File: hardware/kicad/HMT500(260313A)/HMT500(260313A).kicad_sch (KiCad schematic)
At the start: 0 parts

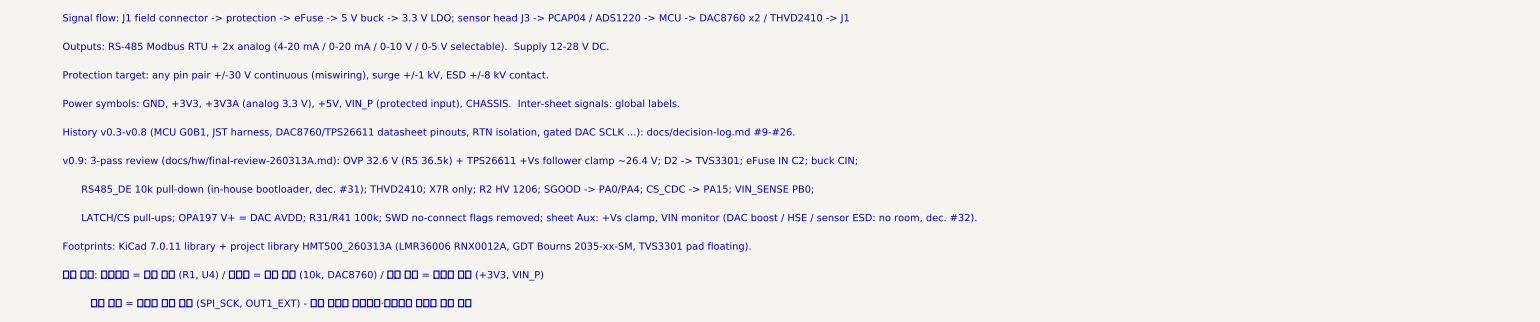
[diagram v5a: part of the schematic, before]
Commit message: Apply agreed external review items (decision #35)
- H01: series 100 V Schottky D3 (PMEG10010ELR) between D2 and eFuse IN
  (new net VIN_D) so negative surges no longer stress U1 IN-OUT
- H02: RS-485 bus TVS D60/D61 (TVS3301); U11 -> THVD2410DGKR (VSSOP-8)
- H04: +Vs clamp zener 27 V -> 24 V (BZX84C24LT1G)
- H08: ADS1220 IDAC fixed at 250 uA
- Room for new parts: C7 removed, 37 low-voltage R/C moved to 0402
  (LCSC basic where available); chassis parts keep CH_GAP between each other
- Placement 104/104, netlist 78/78, pcbnew DRC: no clearance errors,
  assembly sim 23 OK; parts list / JLC BOM updated
- docs/hw/external-review-response-260930.md: item responses, output load
  table, current budget, firmware requirements F1-F6, tests T1-T7

Co-Authored-By: Claude Opus 5.5 <noreply@anthropic.com>
Claude-Session: https://claude.ai/code/session_01JA2o8uJsqp9Vzsg4b665ev
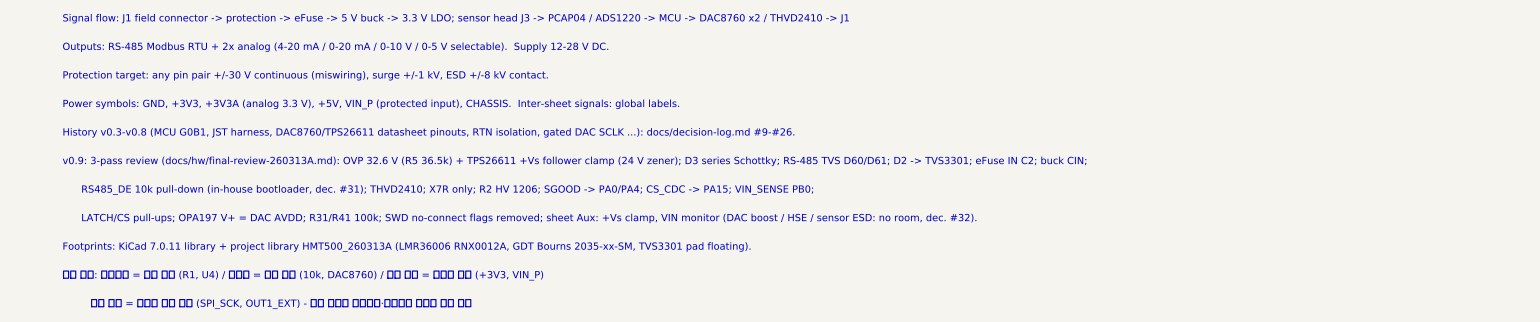
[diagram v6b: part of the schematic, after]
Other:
- note added: "v0.9: 3-pass review (docs/hw/final-review-260313A.md): OVP 32.6 V (R5 36.5k) + TPS26611 +Vs follower clamp (24 V zener); D3 series Schottky; RS-485 TVS D60/D61; D2 -> TVS3301; eFuse IN C2; buck CIN;"
- note removed: "v0.9: 3-pass review (docs/hw/final-review-260313A.md): OVP 32.6 V (R5 36.5k) + TPS26611 +Vs follower clamp ~26.4 V; D2 -> TVS3301; eFuse IN C2; buck CIN;"
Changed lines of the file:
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@@
 (text "Power symbols: GND, +3V3, +3V3A (analog 3.3 V), +5V, VIN_P (protected input), CHASSIS.  Inter-sheet signals: global labels." (at 30.48 177.8 0) (effects (font (size 1.4 1.4)) (justify left bottom)))
 (text "History v0.3-v0.8 (MCU G0B1, JST harness, DAC8760/TPS26611 datasheet pinouts, RTN isolation, gated DAC SCLK ...): docs/decision-log.md #9-#26." (at 30.48 183.388 0) (effects (font (size 1.4 1.4)) (justify left bottom)))
-(text "v0.9: 3-pass review (docs/hw/final-review-260313A.md): OVP 32.6 V (R5 36.5k) + TPS26611 +Vs follower clamp ~26.4 V; D2 -> TVS3301; eFuse IN C2; buck CIN;" (at 30.48 188.976 0) (effects (font (size 1.4 1.4)) (justify left bottom)))
+(text "v0.9: 3-pass review (docs/hw/final-review-260313A.md): OVP 32.6 V (R5 36.5k) + TPS26611 +Vs follower clamp (24 V zener); D3 series Schottky; RS-485 TVS D60/D61; D2 -> TVS3301; eFuse IN C2; buck CIN;" (at 30.48 188.976 0) (effects (font (size 1.4 1.4)) (justify left bottom)))
 (text "      RS485_DE 10k pull-down (in-house bootloader, dec. #31); THVD2410; X7R only; R2 HV 1206; SGOOD -> PA0/PA4; CS_CDC -> PA15; VIN_SENSE PB0;" (at 30.48 194.564 0) (effects (font (size 1.4 1.4)) (justify left bottom)))
 (text "      LATCH/CS pull-ups; OPA197 V+ = DAC AVDD; R31/R41 100k; SWD no-connect flags removed; sheet Aux: +Vs clamp, VIN monitor (DAC boost / HSE / sensor ESD: no room, dec. #32)." (at 30.48 200.152 0) (effects (font (size 1.4 1.4)) (justify left bottom)))

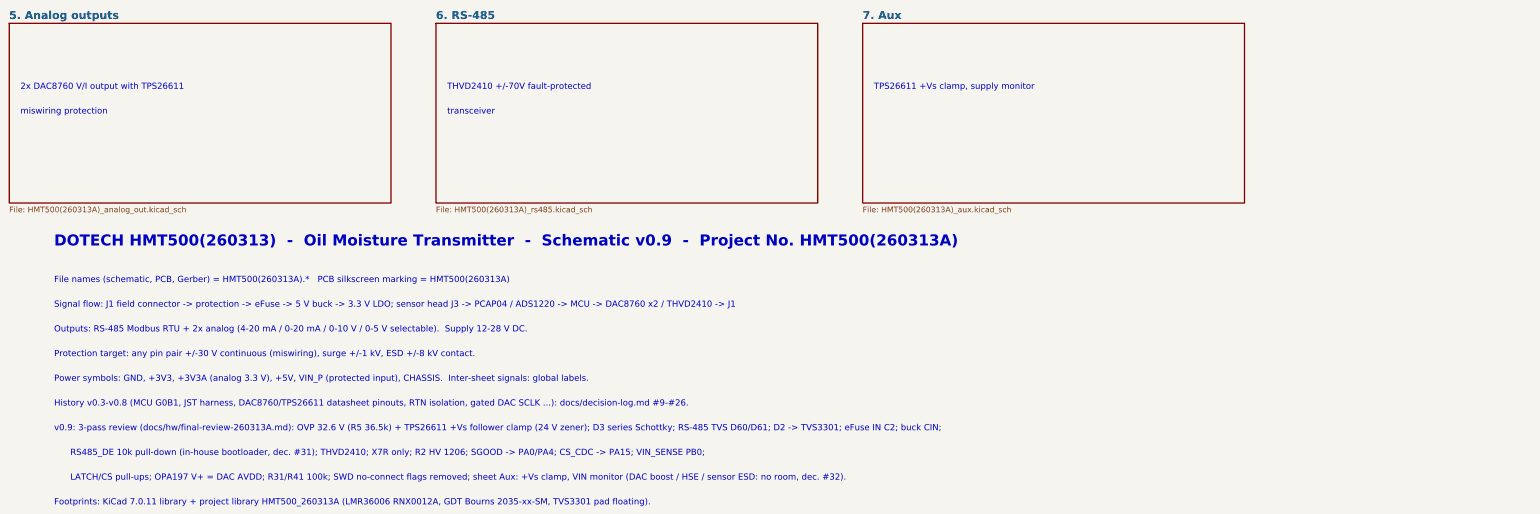
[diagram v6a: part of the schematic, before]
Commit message: Decision #37: fix the DAC section with the IVS320 AO rev 1.0 scheme
- AO supply VAO 16.1 V: LMR51606YFDBVR buck (U15) + 22 uH + 2x10 uF,
  feeding DAC AVDD (via 10 ohm), TPS26611 +Vs and OPA197 V+
- Remove +Vs zener follower (Q1, R50, D50, C53) and C43
- DAC CMP compensation 4.7 nF VOUT-CMP + 100 pF CMP-GND (SBAS528D 8.3.2)
- DAC output clamp BAS70-04 (D41/D51) for protector switching transients
- Output TVS3301 and SGOOD -> MCU ADC kept (+-30 V miswiring requirement)
- 114/114 parts placed, netlist 82/82, DRC no clearance errors,
  assembly sim 23 OK; parts list, JLC BOM, review docs updated

Co-Authored-By: Claude Opus 5.5 <noreply@anthropic.com>
Claude-Session: https://claude.ai/code/session_01JA2o8uJsqp9Vzsg4b665ev
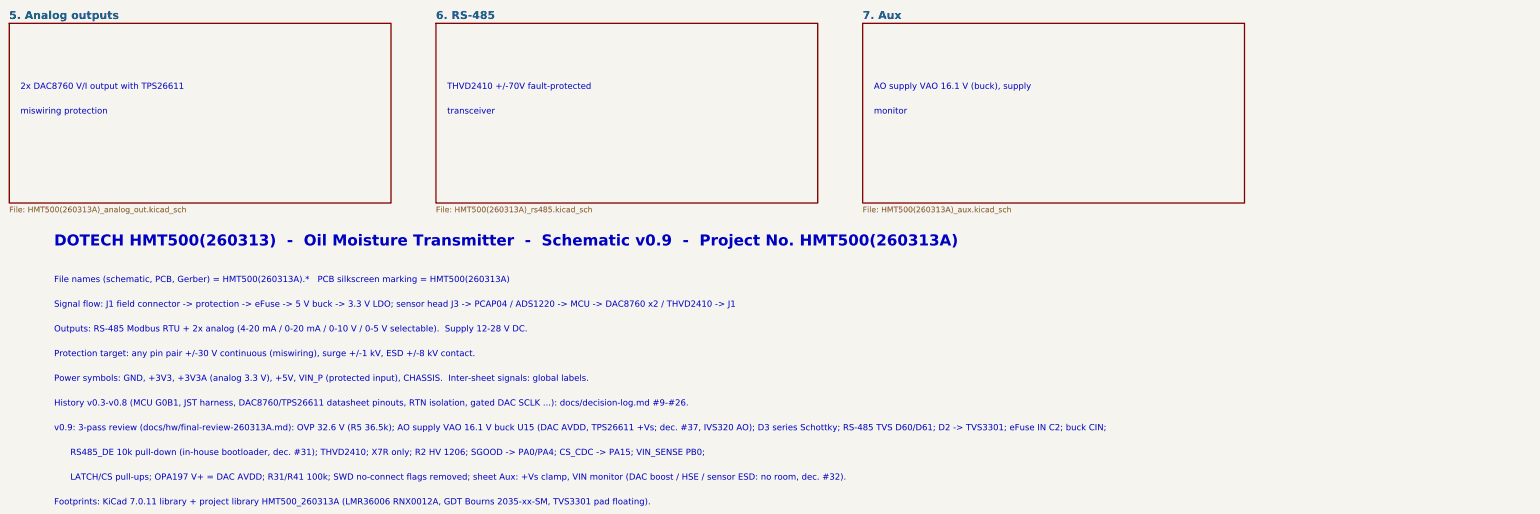
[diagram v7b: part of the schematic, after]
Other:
- note added: "AO supply VAO 16.1 V (buck), supply"
- note added: "monitor"
- note added: "v0.9: 3-pass review (docs/hw/final-review-260313A.md): OVP 32.6 V (R5 36.5k); AO supply VAO 16.1 V buck U15 (DAC AVDD, TPS26611 +Vs; dec. #37, IVS320 AO); D3 series Schottky; RS-485 TVS D60/D61; D2 -> TVS3301; eFuse IN C2; buck CIN;"
- note removed: "TPS26611 +Vs clamp, supply monitor"
- note removed: "v0.9: 3-pass review (docs/hw/final-review-260313A.md): OVP 32.6 V (R5 36.5k) + TPS26611 +Vs follower clamp (24 V zener); D3 series Schottky; RS-485 TVS D60/D61; D2 -> TVS3301; eFuse IN C2; buck CIN;"
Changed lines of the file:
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@@
 (text "transceiver" (at 119.38 117.348 0) (effects (font (size 1.4 1.4)) (justify left bottom)))
 (sheet (at 213.36 96.52) (size 86.36 40.64) (fields_autoplaced) (stroke (width 0.1524) (type solid)) (fill (color 0 0 0 0.0000)) (property "Sheetname" "7. Aux" (at 213.36 95.758 0) (effects (font (size 1.8 1.8) bold) (justify left bottom))) (property "Sheetfile" "HMT500(260313A)_aux.kicad_sch" (at 213.36 137.922 0) (effects (font (size 1.27 1.27)) (justify left top))) (instances (project "HMT500(260313A)" (path "/1ebb025b-11bd-5f7c-aaab-41e2a750e8b3" (page "8")))))
-(text "TPS26611 +Vs clamp, supply monitor" (at 215.9 111.76 0) (effects (font (size 1.4 1.4)) (justify left bottom)))
+(text "AO supply VAO 16.1 V (buck), supply" (at 215.9 111.76 0) (effects (font (size 1.4 1.4)) (justify left bottom)))
+(text "monitor" (at 215.9 117.348 0) (effects (font (size 1.4 1.4)) (justify left bottom)))
 (text "DOTECH HMT500(260313)  -  Oil Moisture Transmitter  -  Schematic v0.9  -  Project No. HMT500(260313A)" (at 30.48 147.32 0) (effects (font (size 2.5 2.5) bold) (justify left bottom)))
 (text "File names (schematic, PCB, Gerber) = HMT500(260313A).*   PCB silkscreen marking = HMT500(260313A)" (at 30.48 155.448 0) (effects (font (size 1.4 1.4)) (justify left bottom)))
@@
 (text "Power symbols: GND, +3V3, +3V3A (analog 3.3 V), +5V, VIN_P (protected input), CHASSIS.  Inter-sheet signals: global labels." (at 30.48 177.8 0) (effects (font (size 1.4 1.4)) (justify left bottom)))
 (text "History v0.3-v0.8 (MCU G0B1, JST harness, DAC8760/TPS26611 datasheet pinouts, RTN isolation, gated DAC SCLK ...): docs/decision-log.md #9-#26." (at 30.48 183.388 0) (effects (font (size 1.4 1.4)) (justify left bottom)))
-(text "v0.9: 3-pass review (docs/hw/final-review-260313A.md): OVP 32.6 V (R5 36.5k) + TPS26611 +Vs follower clamp (24 V zener); D3 series Schottky; RS-485 TVS D60/D61; D2 -> TVS3301; eFuse IN C2; buck CIN;" (at 30.48 188.976 0) (effects (font (size 1.4 1.4)) (justify left bottom)))
+(text "v0.9: 3-pass review (docs/hw/final-review-260313A.md): OVP 32.6 V (R5 36.5k); AO supply VAO 16.1 V buck U15 (DAC AVDD, TPS26611 +Vs; dec. #37, IVS320 AO); D3 series Schottky; RS-485 TVS D60/D61; D2 -> TVS3301; eFuse IN C2; buck CIN;" (at 30.48 188.976 0) (effects (font (size 1.4 1.4)) (justify left bottom)))
 (text "      RS485_DE 10k pull-down (in-house bootloader, dec. #31); THVD2410; X7R only; R2 HV 1206; SGOOD -> PA0/PA4; CS_CDC -> PA15; VIN_SENSE PB0;" (at 30.48 194.564 0) (effects (font (size 1.4 1.4)) (justify left bottom)))
 (text "      LATCH/CS pull-ups; OPA197 V+ = DAC AVDD; R31/R41 100k; SWD no-connect flags removed; sheet Aux: +Vs clamp, VIN monitor (DAC boost / HSE / sensor ESD: no room, dec. #32)." (at 30.48 200.152 0) (effects (font (size 1.4 1.4)) (justify left bottom)))

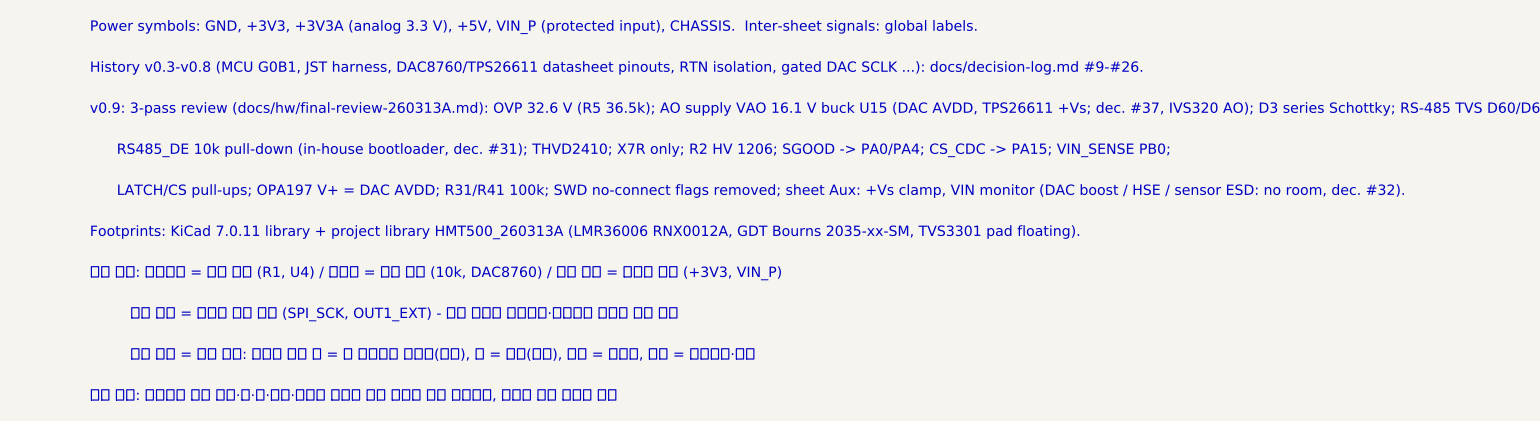
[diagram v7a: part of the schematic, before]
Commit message: Decision #38: prefer JLCPCB parts - U2 LMR51606, R19 0.1 %, std 2512
- 5 V buck U2: LMR36006BRNXR -> LMR51606YFDBVR (same IC as VAO buck),
  L2 10 uH, C6 22 uF, R8/R9 118k/22.1k -> 5.07 V; C9, C10, C11, C17 removed
- R19 -> ERA-3AEB4021V (0.1 %, 25 ppm); R1/R30/R40 -> CRCW2512 standard
- LCSC numbers for 422k and 118k; 57 of 60 BOM lines have LCSC numbers
- 110/110 placed, netlist 81/81, DRC no clearance errors, assembly sim OK

Co-Authored-By: Claude Opus 5.5 <noreply@anthropic.com>
Claude-Session: https://claude.ai/code/session_01JA2o8uJsqp9Vzsg4b665ev
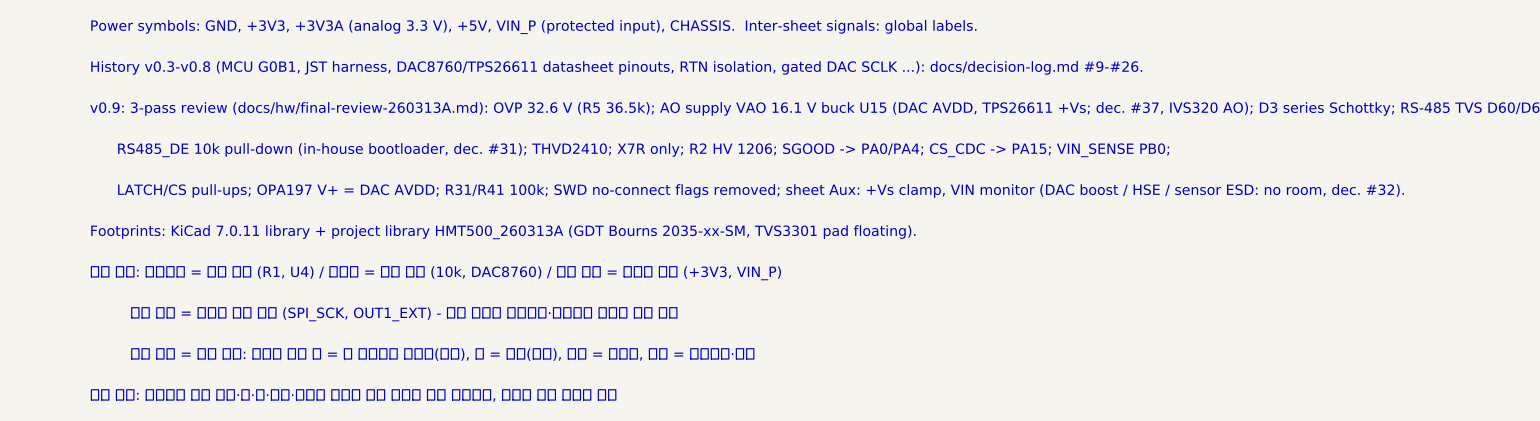
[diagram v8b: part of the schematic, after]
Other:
- note added: "Footprints: KiCad 7.0.11 library + project library HMT500_260313A (GDT Bourns 2035-xx-SM, TVS3301 pad floating)."
- note removed: "Footprints: KiCad 7.0.11 library + project library HMT500_260313A (LMR36006 RNX0012A, GDT Bourns 2035-xx-SM, TVS3301 pad floating)."
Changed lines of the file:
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@@
 (text "      RS485_DE 10k pull-down (in-house bootloader, dec. #31); THVD2410; X7R only; R2 HV 1206; SGOOD -> PA0/PA4; CS_CDC -> PA15; VIN_SENSE PB0;" (at 30.48 194.564 0) (effects (font (size 1.4 1.4)) (justify left bottom)))
 (text "      LATCH/CS pull-ups; OPA197 V+ = DAC AVDD; R31/R41 100k; SWD no-connect flags removed; sheet Aux: +Vs clamp, VIN monitor (DAC boost / HSE / sensor ESD: no room, dec. #32)." (at 30.48 200.152 0) (effects (font (size 1.4 1.4)) (justify left bottom)))
-(text "Footprints: KiCad 7.0.11 library + project library HMT500_260313A (LMR36006 RNX0012A, GDT Bourns 2035-xx-SM, TVS3301 pad floating)." (at 30.48 205.74 0) (effects (font (size 1.4 1.4)) (justify left bottom)))
+(text "Footprints: KiCad 7.0.11 library + project library HMT500_260313A (GDT Bourns 2035-xx-SM, TVS3301 pad floating)." (at 30.48 205.74 0) (effects (font (size 1.4 1.4)) (justify left bottom)))
 (text "표기 규칙: 부품번호 = 굵은 글자 (R1, U4) / 부품값 = 보통 글자 (10k, DAC8760) / 전원 네트 = 기울인 글자 (+3V3, VIN_P)" (at 30.48 211.328 0) (effects (font (face "NanumGothic") (size 1.4 1.4)) (justify left bottom)))
 (text "         신호 네트 = 테두리 있는 라벨 (SPI_SCK, OUT1_EXT) - 네트 이름은 부품번호·부품명과 겹치지 않게 지음" (at 30.48 216.916 0) (effects (font (face "NanumGothic") (size 1.4 1.4)) (justify left bottom)))
